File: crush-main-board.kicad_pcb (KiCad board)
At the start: 2 copper layers, 101.6 x 120.6 mm, 46 parts, among them J1 4x4_Header, J10 3x3 Header, J11 3x3 Header, J12 3x2 Header, J13 3x4_Header, J14 3x4_Header, J15 2157601008, J16 Conn_01x02, J17 Conn_01x02, J2 4x4_Header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

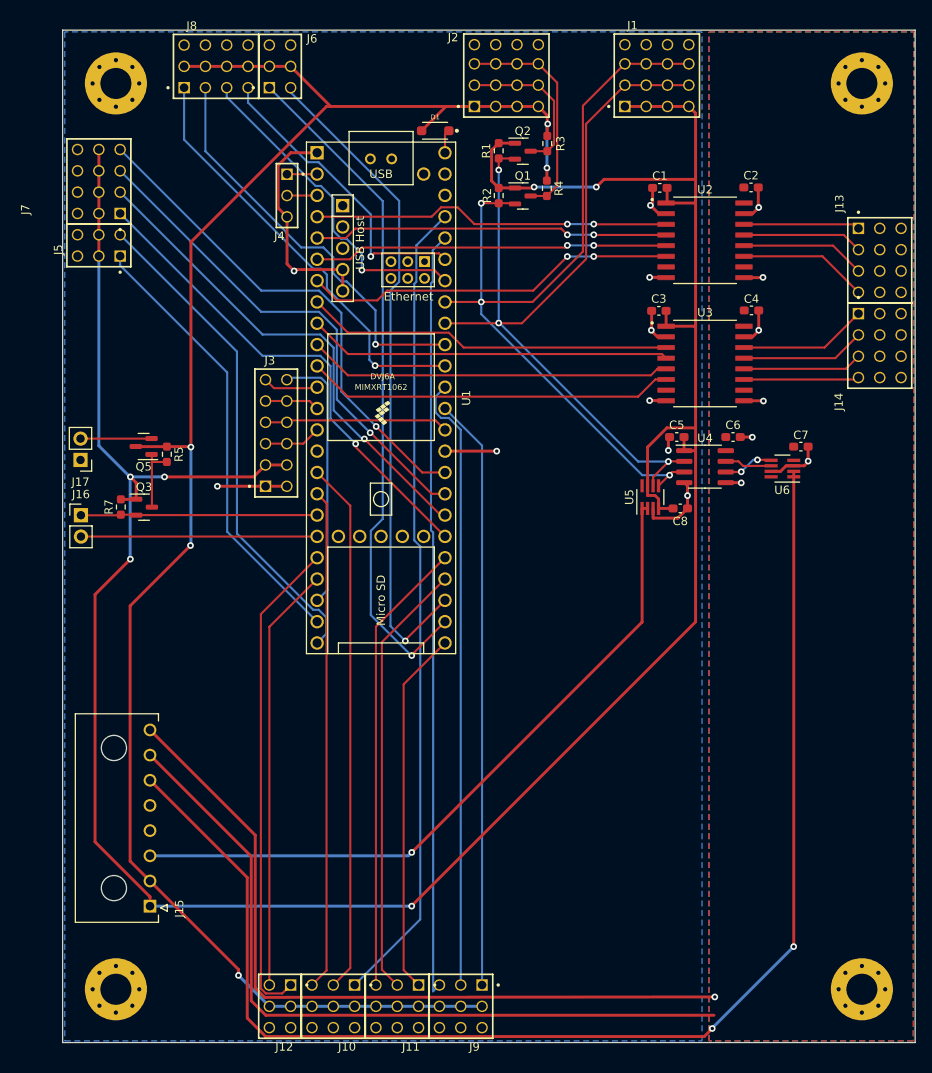
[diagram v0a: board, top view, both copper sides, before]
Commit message: Updated main board for better bypass caps & routing review
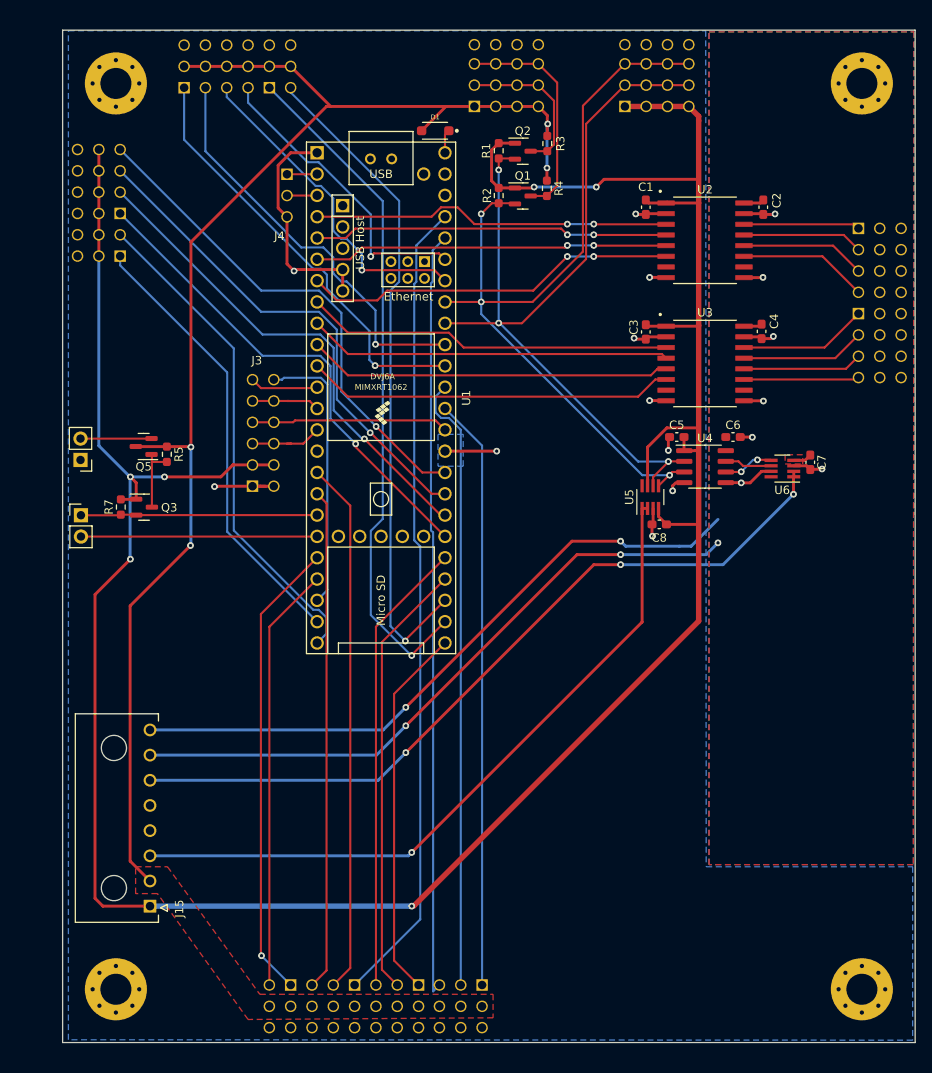
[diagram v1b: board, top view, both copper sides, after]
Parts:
- moved C8 3.15 mm to (83.8, 71.6), turned to 0 degrees
- moved C3 2.95 mm to (82.2, 48.7), turned to 90 degrees
- moved C1 2.85 mm to (82.2, 33.8), turned to 90 degrees
- moved C4 2.78 mm to (96.0, 48.6), turned to 90 degrees
- moved C2 2.77 mm to (96.2, 33.8), turned to 90 degrees
- moved C7 2.18 mm to (101.8, 64.2), turned to 90 degrees
- moved J3 1.55 mm to (36.6, 60.7)
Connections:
- net +RELAY renamed /+RELAY
- J17 pad 1: -RELAY -> GND
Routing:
- net BATT_T: track 160.3 -> 93.5 mm, vias 2 -> 3
- net +5V: track 215.6 -> 169.4 mm, vias 5 -> 4
- net GND_T: track 115.4 -> 102.3 mm, vias 8 -> 9
- net +3V3_T: track 90.1 -> 85.1 mm, vias 0 -> 3
- net +3V3: track 331.5 -> 336.2 mm
- net GND: track 65.2 -> 60.5 mm, vias 9 -> 10
- net PWM28: track 58.3 -> 55.3 mm, vias 0 -> 1
- net SPI_SDI: track 6.83 -> 8.86 mm
- net SPI_SDO: track 6.52 -> 8.35 mm
- net SPI_SCK: track 21.9 -> 23.5 mm
- net DIO30: track 31.5 -> 33.1 mm
- net SPI_CS: track 6.61 -> 8.16 mm
- net PWM33: track 43.5 -> 44.5 mm
- net SCL_3V3: track 102.4 -> 101.7 mm
- added copper zone on F.Cu, net +5V

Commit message: cleanup traces
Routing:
- net PWM22: track 91.6 -> 90.1 mm
- net +3V3: track 336.2 -> 336.9 mm

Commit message: silkscreen
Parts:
- added G***: LOGO, LOGO, F.Cu at (89.5, 115.5)
- moved J5 3.45 mm to (17.0, 41.8)
- moved J7 3.45 mm to (17.0, 34.2)
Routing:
- net +3V3: track 336.9 -> 333.0 mm
- net DIO32: track 59.7 -> 58.3 mm
- net DIO31: track 53.3 -> 51.9 mm
- net A/DIO41: track 60.2 -> 58.8 mm
- net A/DIO39: track 59.0 -> 57.6 mm
- net A/DIO38: track 58.6 -> 57.2 mm
- net A/DIO40: track 59.5 -> 58.1 mm
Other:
- board text added: "+"
- board text added: "-"
- board text added: "14"
- board text added: "15"
- board text added: "16"
- board text added: "17"
- board text added: "20"
- board text added: "21"
- board text added: "22"
- board text added: "23"
- board text added: "24"
- board text added: "25"
- board text added: "28"
- board text added: "29"
- board text added: "31"
- board text added: "32"
- board text added: "33"
- board text added: "34"
- board text added: "35"
- board text added: "36"
- board text added: "37"
- board text added: "38"
- board text added: "39"
- board text added: "3V3"
- board text added: "3V3_T"
- board text added: "40"
- board text added: "41"
- board text added: "5V"
- board text added: "BATT"
- board text added: "BATT_T"
- board text added: "CS"
- board text added: "DIO"
- board text added: "DIO 30"
- board text added: "DIO/A"
- board text added: "GND"
- board text added: "GND_T"
- board text added: "HBL (7)"
- board text added: "HBR (5)"
- board text added: "HFL (8)"
- board text added: "HFR (4)"
- board text added: "HW Kill"
- board text added: "I2C"
- board text added: "PWM"
- board text added: "RELAY"
- board text added: "RX"
- board text added: "SCK"
- board text added: "SCL"
- board text added: "SD0"
- board text added: "SDA"
- board text added: "SDI"
- board text added: "SPI"
- board text added: "Signal Board Rev. 1"
- board text added: "THRUSTER PWM"
- board text added: "TX"
- board text added: "To Power Board"
- board text added: "UART"
- board text added: "VBL (9)"
- board text added: "VBR (3)"
- board text added: "VFL (6)"
- board text added: "VFR (2)"

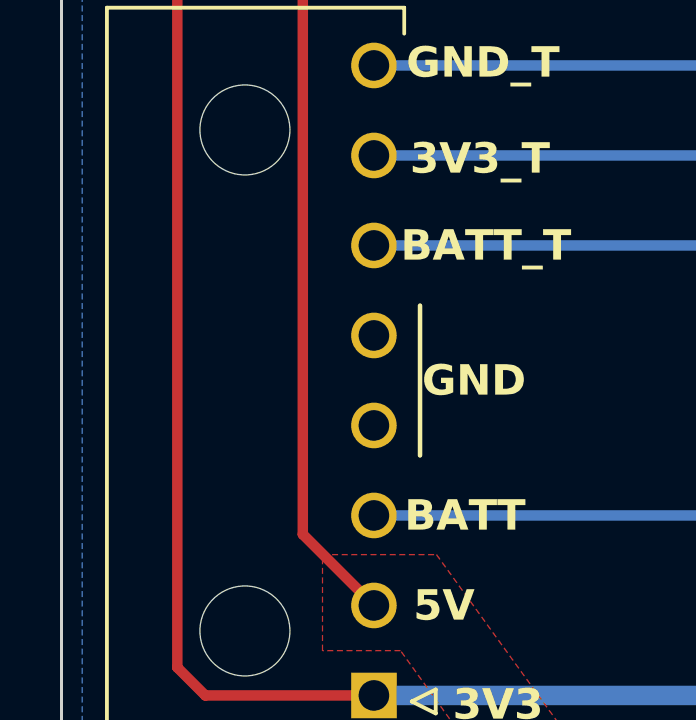
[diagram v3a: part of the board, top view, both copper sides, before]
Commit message: add JLC order number location
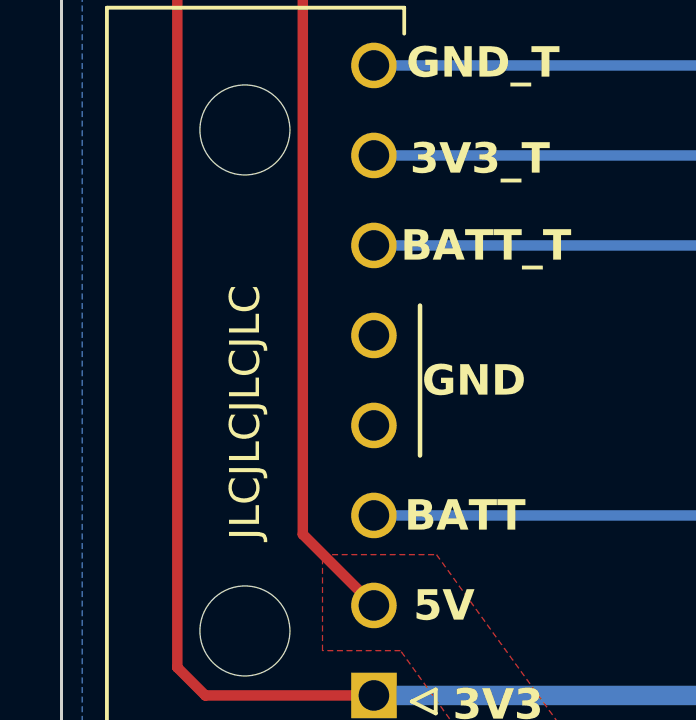
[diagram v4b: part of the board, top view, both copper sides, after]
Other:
- board text added: "JLCJLCJLCJLC"
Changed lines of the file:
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@@
+    (effects (font (size 1 1) (thickness 0.15)) (justify left bottom))
+  )
+  (gr_text "JLCJLCJLCJLC" (at 19.4056 111.9124 90) (layer "F.SilkS")
     (effects (font (size 1 1) (thickness 0.15)) (justify left bottom))
   )

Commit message: add additional labeling to io ports
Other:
- board text added: "S"
- board text added: "V"
- board text added: "⏚"
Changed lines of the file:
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@@
     )
   )
-  (gr_rect (start 100.1268 31.5976) (end 113.8936 55.4228)
+  (gr_rect (start 100.1268 31.5976) (end 113.8936 57.3532)
     (stroke (width 0.15) (type default)) (fill none) (layer "F.SilkS"))
   (gr_line (start 76.0476 14.4272) (end 78.486 14.4272)
@@
   (gr_line (start 22.7076 29.6926) (end 22.7076 38.7604)
     (stroke (width 0.15) (type default)) (layer "F.SilkS"))
-  (gr_rect (start 13.1572 29.1084) (end 26.4668 44.3484)
+  (gr_rect (start 13.1572 29.1084) (end 26.4668 46.4312)
     (stroke (width 0.15) (type default)) (fill none) (layer "F.SilkS"))
   (gr_line (start 22.7076 39.878) (end 22.7076 43.8404)
@@
   (gr_line (start 76.1492 19.2024) (end 78.486 19.2024)
     (stroke (width 0.15) (type default)) (layer "F.SilkS"))
-  (gr_rect (start 36.0299 120.9548) (end 63.9572 132.9182)
+  (gr_rect (start 36.0299 120.9548) (end 65.7352 132.9182)
     (stroke (width 0.15) (type default)) (fill none) (layer "F.SilkS"))
   (gr_line (start 70.612 19.2024) (end 72.7964 19.2024)
@@
   (gr_line (start 26.416 22.9108) (end 35.3568 22.9108)
     (stroke (width 0.15) (type default)) (layer "F.SilkS"))
-  (gr_rect (start 25.8064 13.0556) (end 41.148 26.7716)
+  (gr_rect (start 24.0284 13.0556) (end 41.148 26.7716)
     (stroke (width 0.15) (type default)) (fill none) (layer "F.SilkS"))
   (gr_line (start 36.6014 22.9108) (end 40.5892 22.9108)
@@
   (gr_rect (start 12.7 12.7) (end 114.3 133.35)
     (stroke (width 0.1) (type default)) (fill none) (layer "Edge.Cuts"))
+  (gr_text "V" (at 16.3576 44.6024 270) (layer "F.SilkS")
+    (effects (font (size 1 1) (thickness 0.15)) (justify left bottom))
+  )
   (gr_text "GND" (at 72.8472 15.0876) (layer "F.SilkS")
     (effects (font (size 1 1) (thickness 0.15)) (justify left bottom))
@@
     (effects (font (size 1 1) (thickness 0.15)) (justify left bottom))
   )
+  (gr_text "S" (at 107.0102 56.7944) (layer "F.SilkS")
+    (effects (font (size 1 1) (thickness 0.15)) (justify left bottom))
+  )
   (gr_text "GND" (at 31.0896 67.7164) (layer "F.SilkS")
     (effects (font (size 1 1) (thickness 0.15)) (justify left bottom))
@@
     (effects (font (size 1 1) (thickness 0.15)) (justify left bottom))
   )
+  (gr_text "⏚" (at 13.8176 44.3992 -90) (layer "F.SilkS")
+    (effects (font (size 1 1) (thickness 0.15)) (justify left bottom))
+  )
   (gr_text "3V3" (at 27.2508 117.3968) (layer "F.SilkS")
     (effects (font (size 1.016 1.016) (thickness 0.150012) bold))
@@
     (effects (font (size 1 1) (thickness 0.15)) (justify left bottom))
   )
+  (gr_text "V" (at 64.262 129.6416) (layer "F.SilkS")
+    (effects (font (size 1 1) (thickness 0.15)) (justify left bottom))
+  )
   (gr_text "RELAY" (at 18.034 60.2996 270) (layer "F.SilkS")
     (effects (font (size 1 1) (thickness 0.2) bold) (justify left bottom))
   )
   (gr_text "SDA" (at 72.9488 19.812) (layer "F.SilkS")
+    (effects (font (size 1 1) (thickness 0.15)) (justify left bottom))
+  )
+  (gr_text "S" (at 64.2112 127.1524) (layer "F.SilkS")
     (effects (font (size 1 1) (thickness 0.15)) (justify left bottom))
   )
@@
     (effects (font (size 1 1) (thickness 0.15)) (justify left bottom))
   )
+  (gr_text "V" (at 24.5872 17.6784) (layer "F.SilkS")
+    (effects (font (size 1 1) (thickness 0.15)) (justify left bottom))
+  )
   (gr_text "+" (at 16.51 61.8744) (layer "F.SilkS")
     (effects (font (size 1 1) (thickness 0.15)) (justify left bottom))
@@
     (effects (font (size 1 1) (thickness 0.2) bold) (justify left bottom))
   )
+  (gr_text "S" (at 24.5364 20.2184) (layer "F.SilkS")
+    (effects (font (size 1 1) (thickness 0.15)) (justify left bottom))
+  )
+  (gr_text "⏚" (at 64.0588 132.1816) (layer "F.SilkS")
+    (effects (font (size 1 1) (thickness 0.15)) (justify left bottom))
+  )
   (gr_text "DIO" (at 22.9616 40.64 -90) (layer "F.SilkS")
+    (effects (font (size 1 1) (thickness 0.15)) (justify left bottom))
+  )
+  (gr_text "V" (at 109.6264 56.8452) (layer "F.SilkS")
     (effects (font (size 1 1) (thickness 0.15)) (justify left bottom))
   )
@@
     (effects (font (size 1 1) (thickness 0.15)) (justify left bottom))
   )
+  (gr_text "⏚" (at 24.384 15.1892) (layer "F.SilkS")
+    (effects (font (size 1 1) (thickness 0.15)) (justify left bottom))
+  )
   (gr_text "VBL (9)" (at 100.7364 54.6608) (layer "F.SilkS")
     (effects (font (size 1 1) (thickness 0.15)) (justify left bottom))
@@
     (effects (font (size 1.016 1.016) (thickness 0.150012) bold))
   )
+  (gr_text "S" (at 18.8468 44.5516 -90) (layer "F.SilkS")
+    (effects (font (size 1 1) (thickness 0.15)) (justify left bottom))
+  )
   (gr_text "Signal Board Rev. 1" (at 81.5848 125.6284) (layer "F.SilkS")
     (effects (font (size 1 1) (thickness 0.15)) (justify left bottom))
   )
+  (gr_text "⏚" (at 112.014 56.7944) (layer "F.SilkS")
+    (effects (font (size 1 1) (thickness 0.15)) (justify left bottom))
+  )

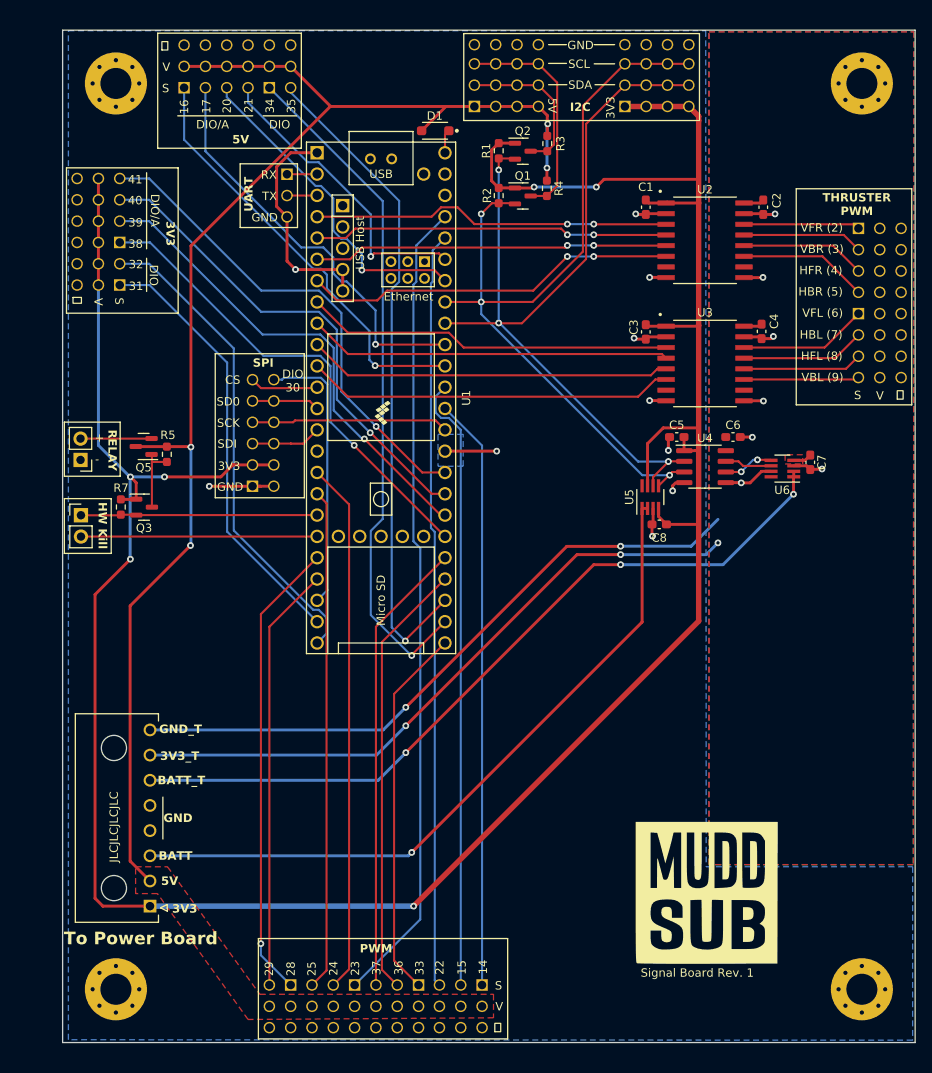
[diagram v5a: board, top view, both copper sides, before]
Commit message: use + instead of V for vcc
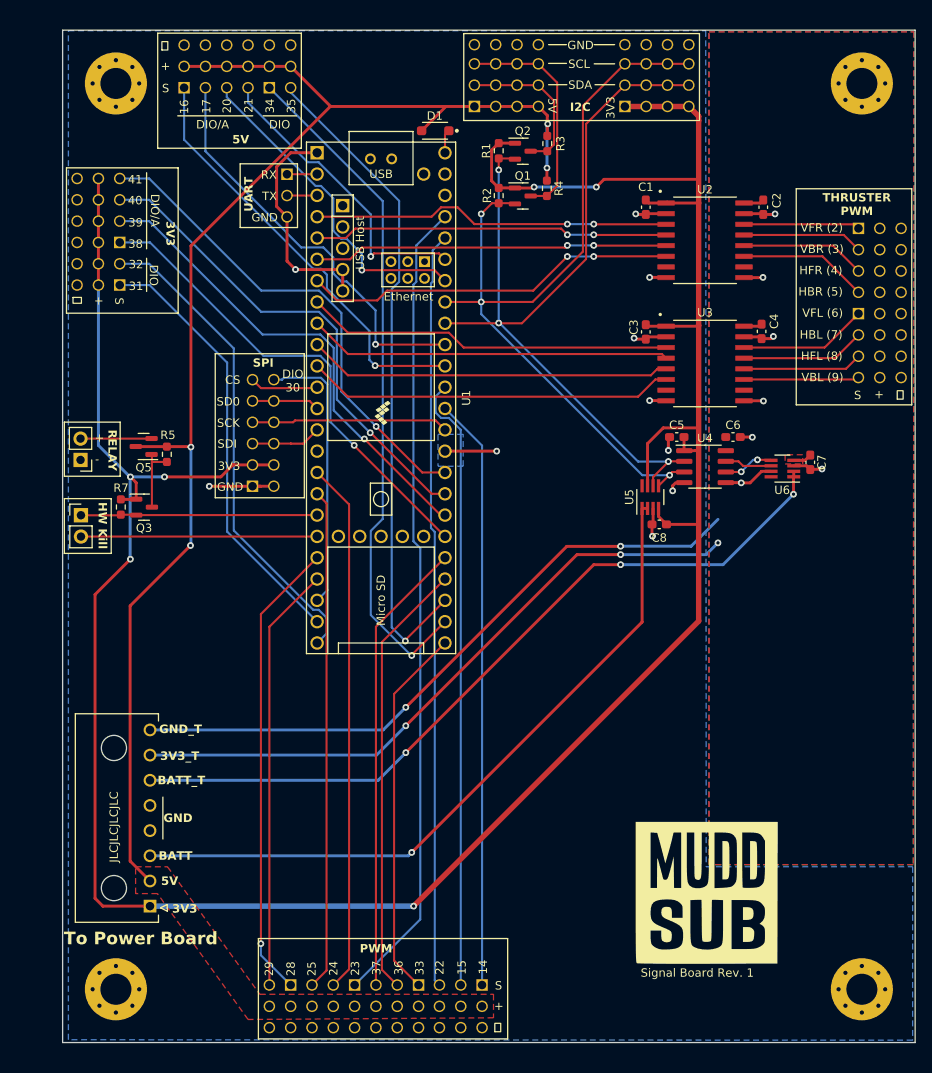
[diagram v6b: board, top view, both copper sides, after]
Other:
- board text removed: "V"
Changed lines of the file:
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@@
   (gr_rect (start 12.7 12.7) (end 114.3 133.35)
     (stroke (width 0.1) (type default)) (fill none) (layer "Edge.Cuts"))
-  (gr_text "V" (at 16.3576 44.6024 270) (layer "F.SilkS")
+  (gr_text "+" (at 16.4592 44.3992 270) (layer "F.SilkS")
     (effects (font (size 1 1) (thickness 0.15)) (justify left bottom))
   )
@@
     (effects (font (size 1 1) (thickness 0.15)) (justify left bottom))
   )
-  (gr_text "V" (at 64.262 129.6416) (layer "F.SilkS")
+  (gr_text "+" (at 64.1096 129.5908) (layer "F.SilkS")
     (effects (font (size 1 1) (thickness 0.15)) (justify left bottom))
   )
@@
     (effects (font (size 1 1) (thickness 0.15)) (justify left bottom))
   )
-  (gr_text "V" (at 24.5872 17.6784) (layer "F.SilkS")
+  (gr_text "+" (at 24.384 17.5768) (layer "F.SilkS")
     (effects (font (size 1 1) (thickness 0.15)) (justify left bottom))
   )
@@
     (effects (font (size 1 1) (thickness 0.15)) (justify left bottom))
   )
-  (gr_text "V" (at 109.6264 56.8452) (layer "F.SilkS")
+  (gr_text "+" (at 109.4232 56.6928) (layer "F.SilkS")
     (effects (font (size 1 1) (thickness 0.15)) (justify left bottom))
   )
